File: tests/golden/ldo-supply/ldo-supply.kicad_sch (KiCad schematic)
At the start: 7 parts, among them J1 CONN_PWR_1X02, J2 CONN_PWR_1X02, U1 AMS1117_3V3

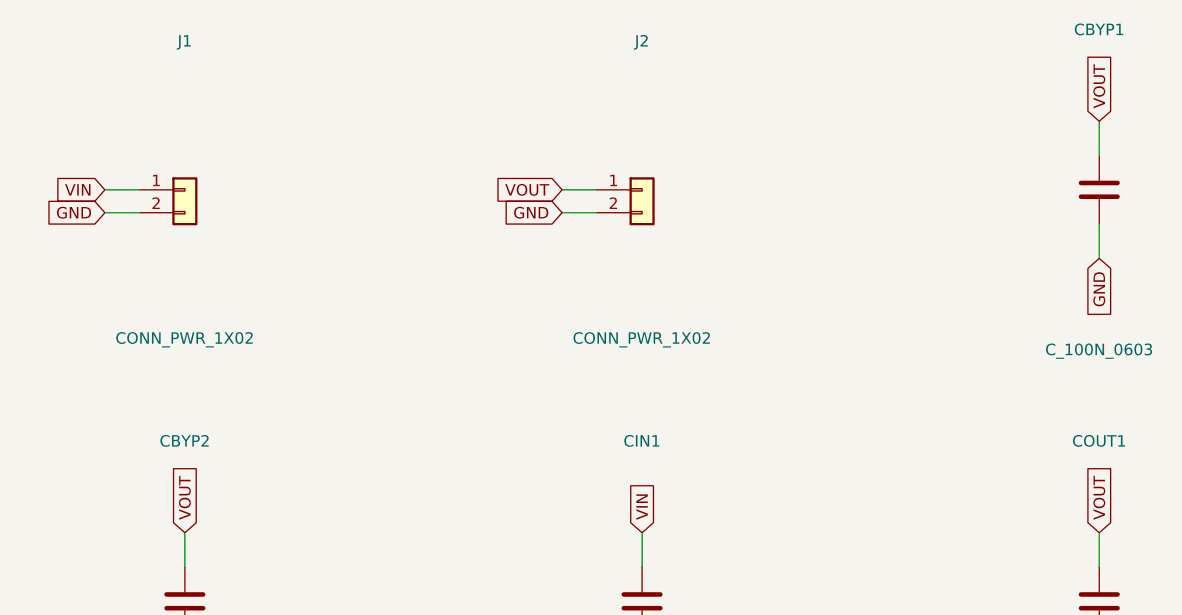
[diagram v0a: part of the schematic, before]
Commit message: M5: partial reads of a design, for token economy
`aipcb summary` gives a one-line-per-block overview, and `aipcb query` narrows to
one module, component, net, net class or role. All take --json, and text and JSON
render the same structure so they cannot disagree about what a design contains.

`query module` includes the components on the *other* side of the module's ports.
A module read in isolation says nothing about what it drives, and that context is
usually the reason it is being read at all.

Also fixes automatic designator assignment. Auto-numbered parts inside a module
took their prefix from the source name, so the LDO's input capacitor became CIN1
rather than C1. Valid, but BOM tools, pick-and-place files and assembly houses all
read the prefix as the component class. Parts now carry an optional
`refdes_prefix`, which is deliberately not read from the KiCad symbol: that would
make designators depend on whether KiCad is installed, and the same source has to
produce the same board everywhere.

Co-Authored-By: Claude Opus 5 (1M context) <noreply@anthropic.com>
Claude-Session: https://claude.ai/code/session_01KUjvxrMBoskX2uCYLqdAeR
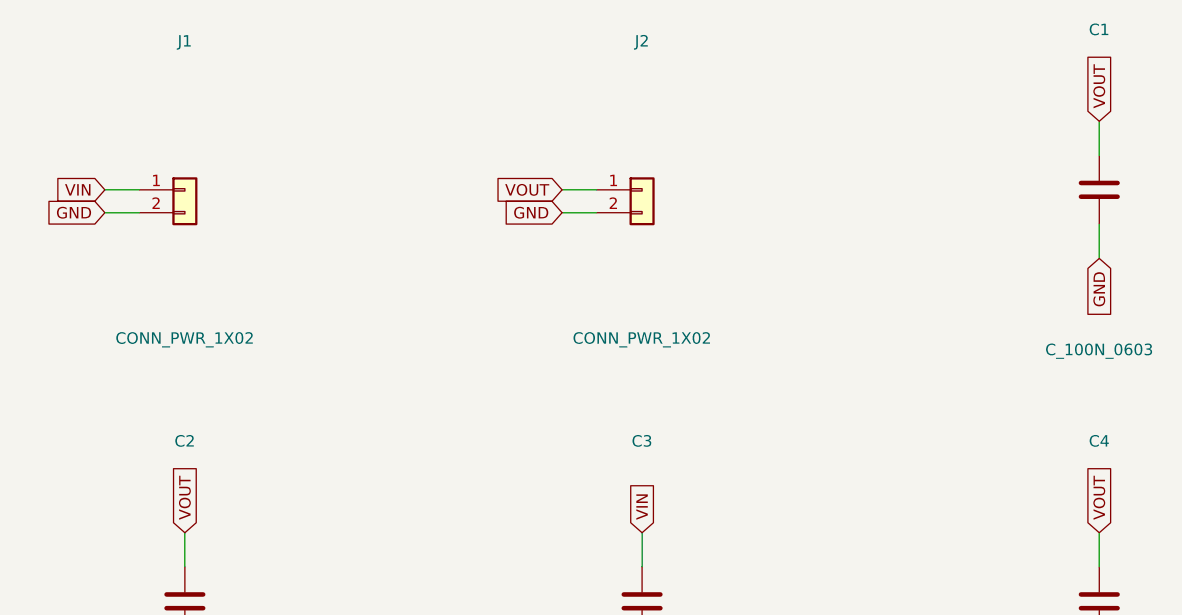
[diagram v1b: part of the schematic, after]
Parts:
- renumbered CBYP1 to C1, CBYP2 to C2, CIN1 to C3, COUT1 to C4
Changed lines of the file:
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@@
 		(on_board yes)
 		(dnp no)
-		(property "Reference" "CBYP1"
+		(property "Reference" "C1"
 			(at 152.4 30.48 0)
 			(effects
@@
 			(project "ldo-supply"
 				(path "/fac7359a-0697-5d85-9732-947d62b06bc7"
-					(reference "CBYP1")
+					(reference "C1")
 					(unit 1)
 				)
@@
 		(on_board yes)
 		(dnp no)
-		(property "Reference" "CBYP2"
+		(property "Reference" "C2"
 			(at 50.8 76.2 0)
 			(effects
@@
 			(project "ldo-supply"
 				(path "/fac7359a-0697-5d85-9732-947d62b06bc7"
-					(reference "CBYP2")
+					(reference "C2")
 					(unit 1)
 				)
@@
 		(on_board yes)
 		(dnp no)
-		(property "Reference" "CIN1"
+		(property "Reference" "C3"
 			(at 101.6 76.2 0)
 			(effects
@@
 			(project "ldo-supply"
 				(path "/fac7359a-0697-5d85-9732-947d62b06bc7"
-					(reference "CIN1")
+					(reference "C3")
 					(unit 1)
 				)
@@
 		(on_board yes)
 		(dnp no)
-		(property "Reference" "COUT1"
+		(property "Reference" "C4"
 			(at 152.4 76.2 0)
 			(effects
@@
 			(project "ldo-supply"
 				(path "/fac7359a-0697-5d85-9732-947d62b06bc7"
-					(reference "COUT1")
+					(reference "C4")
 					(unit 1)
 				)

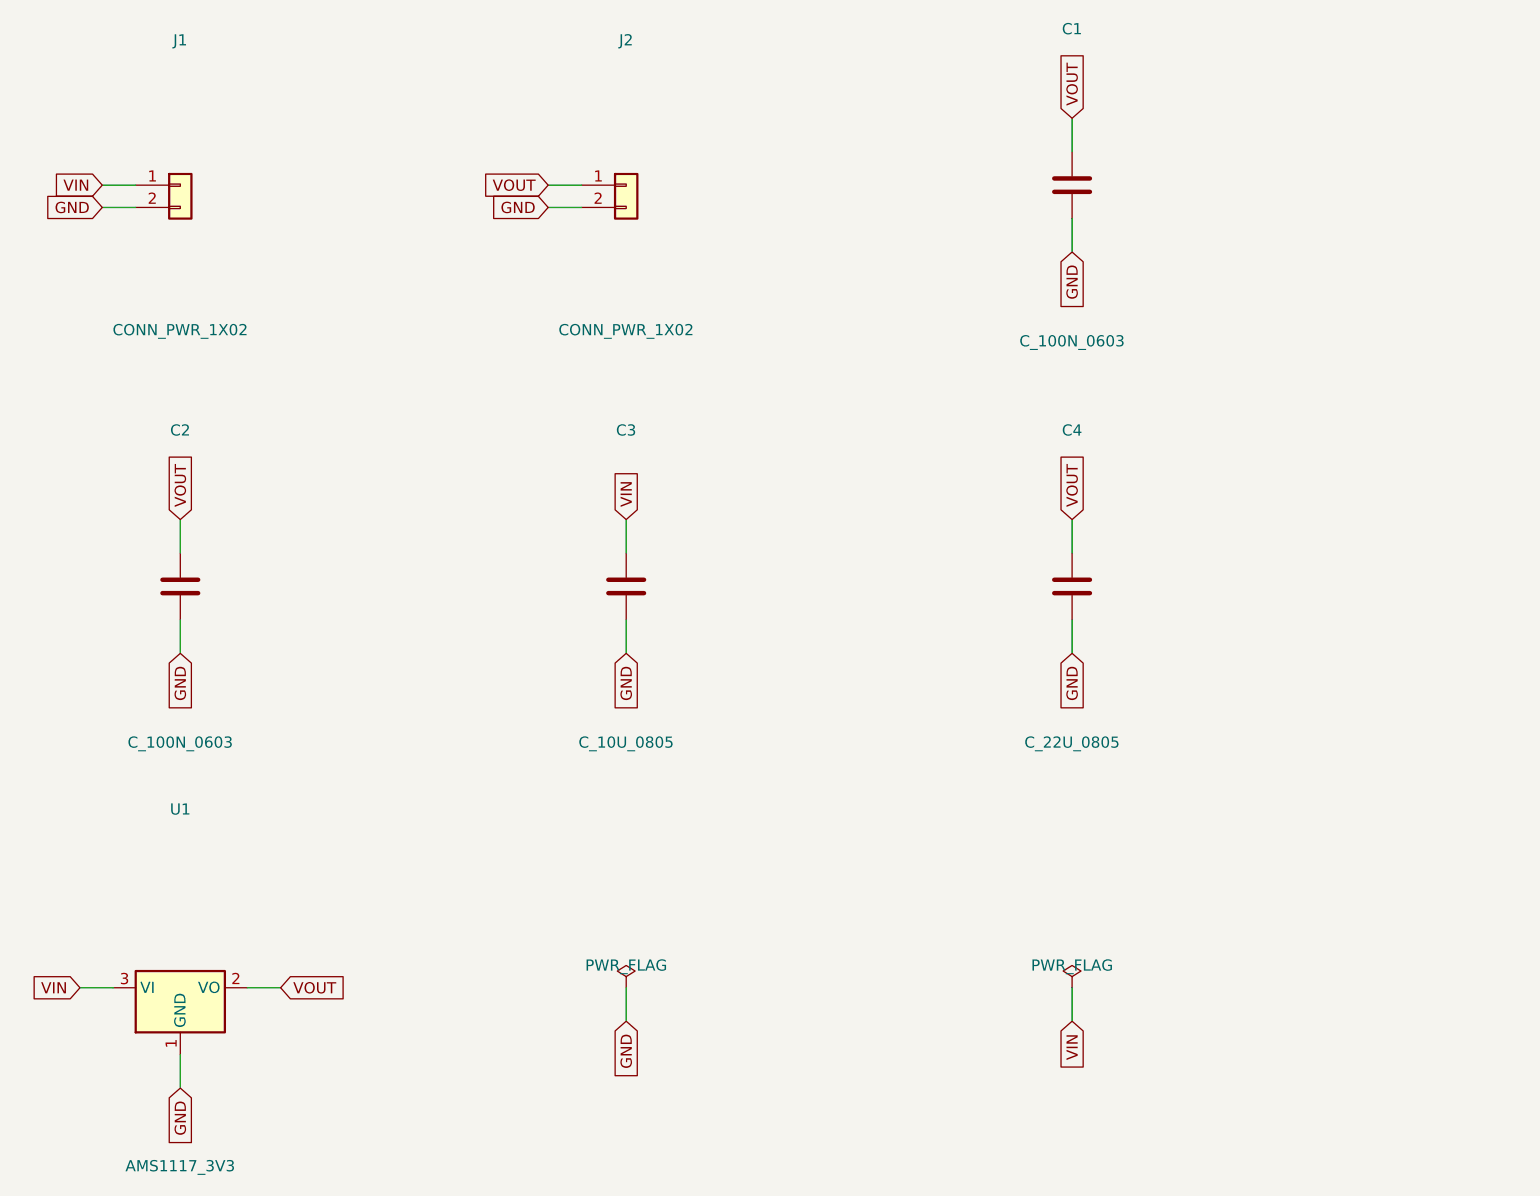
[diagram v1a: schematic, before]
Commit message: M14: the sheet that could not be reviewed, and the router that was never asked
Two themes. The generated schematics were electrically correct and unreadable:
every fact the source knew about *why* a part exists -- `role`, `for:`, the module
hierarchy, the netlist graph -- died at the sheet boundary, and a capacitor whose
purpose is to sit at one pin of one IC was placed by its position in a sorted list.
On pcie-sata that was 157.5 mm from the pin it decouples, on a sheet 594 mm wide.
And manual routing was something that *happened* to a board rather than something
the source could declare.

Placement is now derived in five steps (aipcb/compile/sheet.py): satellites attach
to what they serve, module instances become named clusters, blocks are ranked left
to right by breadth-first distance over signal nets only, ordered by a barycentre
sweep, and placed by measured extents. Rails point up, grounds point down, and a
crowded pin row keeps its labels because a ground symbol is wider than a 2.54 mm
pitch.

Measured across all eleven examples, before -> after:

  overlapping drawn items            71 -> 0
  mean decoupling-to-IC distance     down on every example with a local cap
    pcie-sata                     157.5 -> 27.8 mm
  total wire length                1196 -> 1151 mm
  wire crossings                      0 -> 0   (a stub idiom has none; said so)
  pcie-sata paper                    A1 -> A3

Nothing electrical moved, and it is proved rather than asserted: KiCad's own
netlister run against the pre- and post-M14 sheets agrees net name for net name and
pin for pin on all eleven; ERC is still 0; two builds are byte-identical; and
regenerating the golden tree moved eleven files, all of them .kicad_sch.

Three defects the *measurement* found, not the eye: KiCad's libraries stack a
part's repeated power pins on one coordinate and we drew nine identical GND labels
there; reference and value text was placed from the pin field rather than from the
drawing; and a block a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
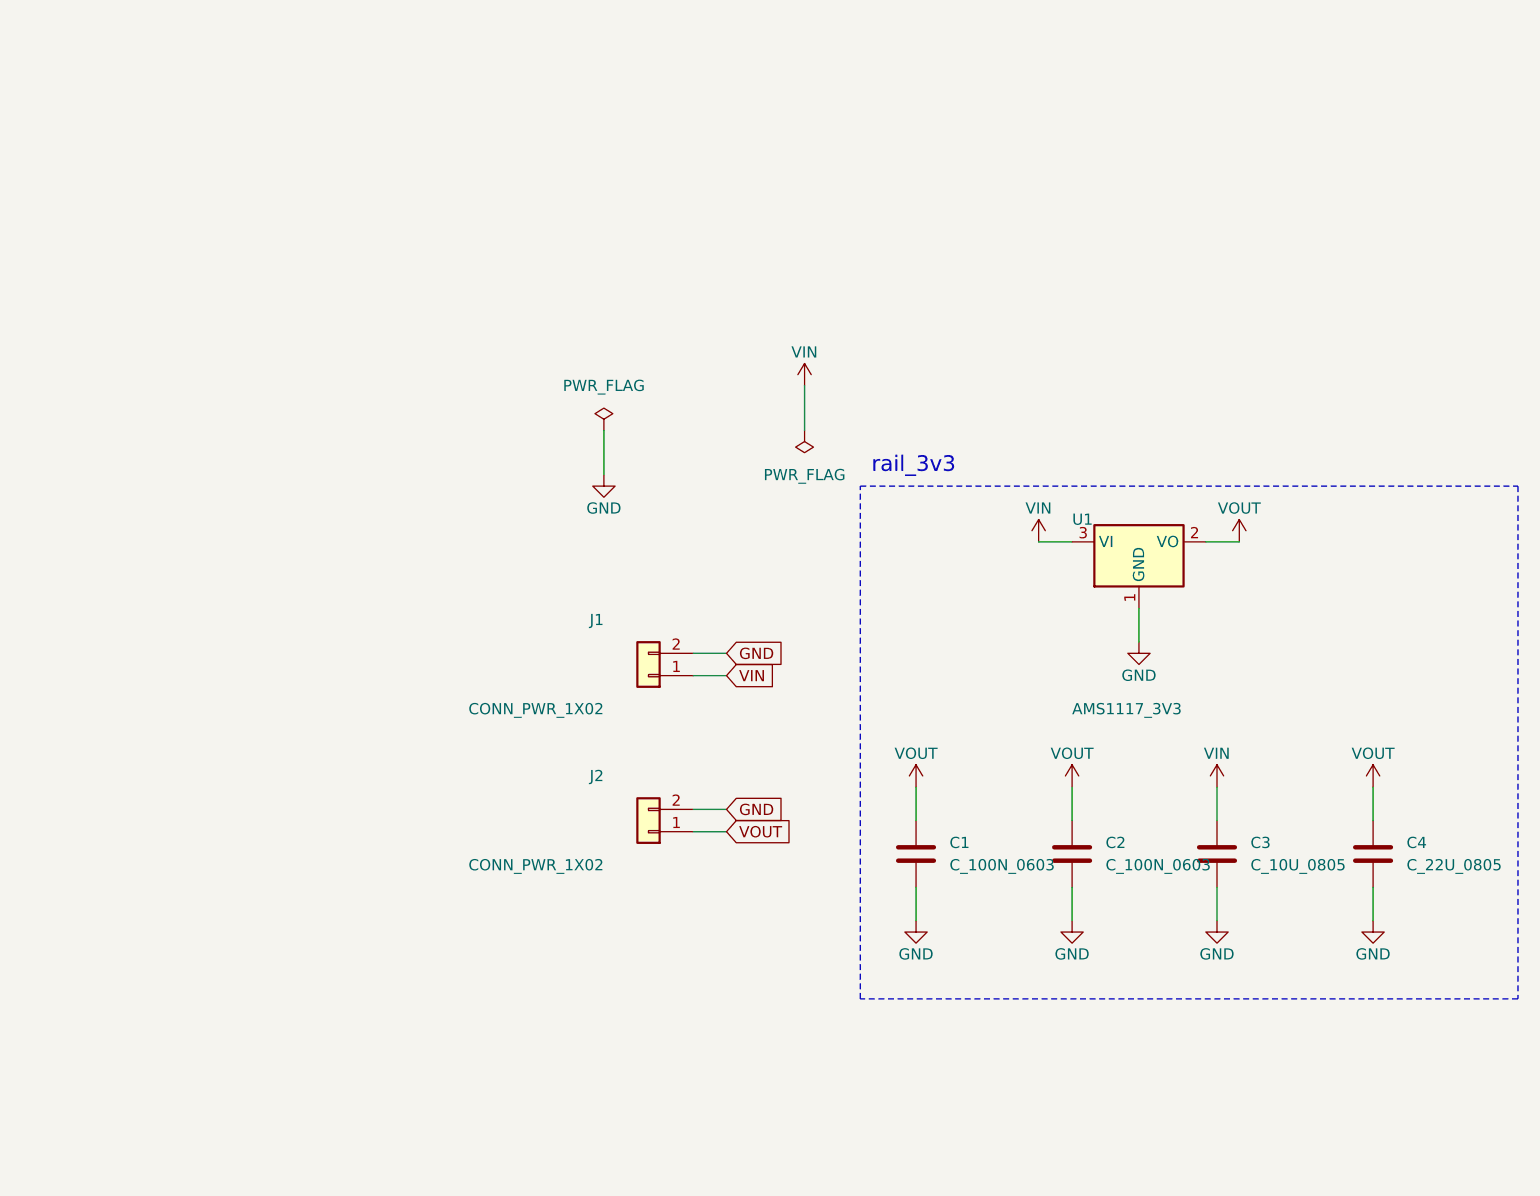
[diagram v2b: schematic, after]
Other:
- note added: "rail_3v3"
- moved on the sheet: C1, C2, C3, C4, J1, J2, U1
